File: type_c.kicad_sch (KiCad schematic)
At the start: 14 parts, among them U12 FUSB302B, U14 DPO2036

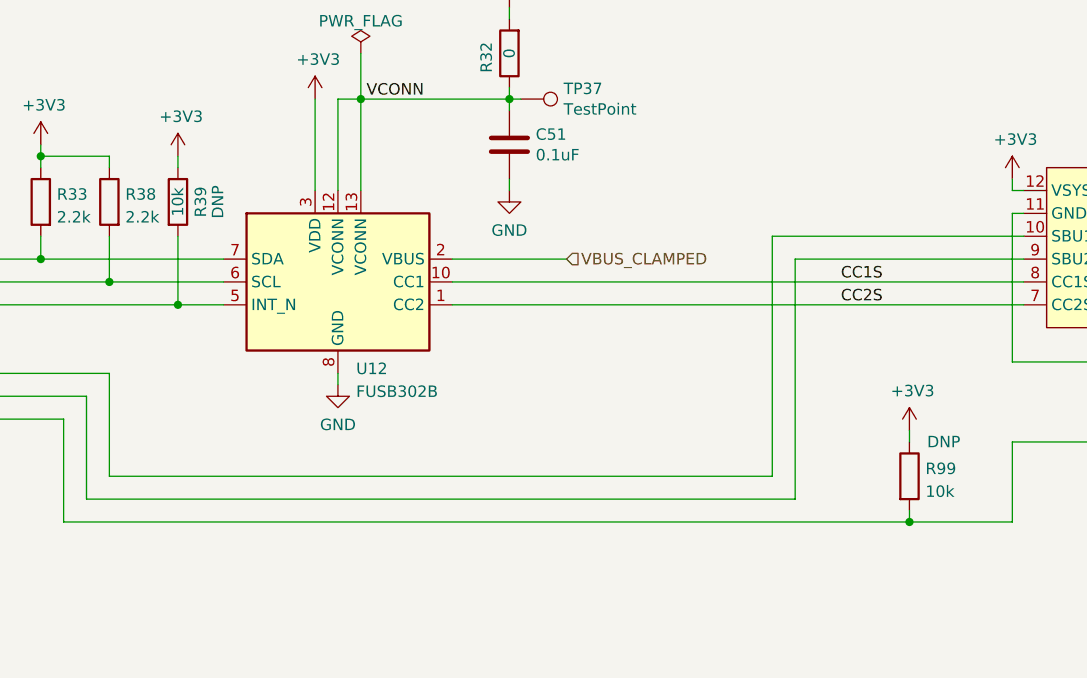
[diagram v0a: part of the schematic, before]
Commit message: add first round of hits on lcsc
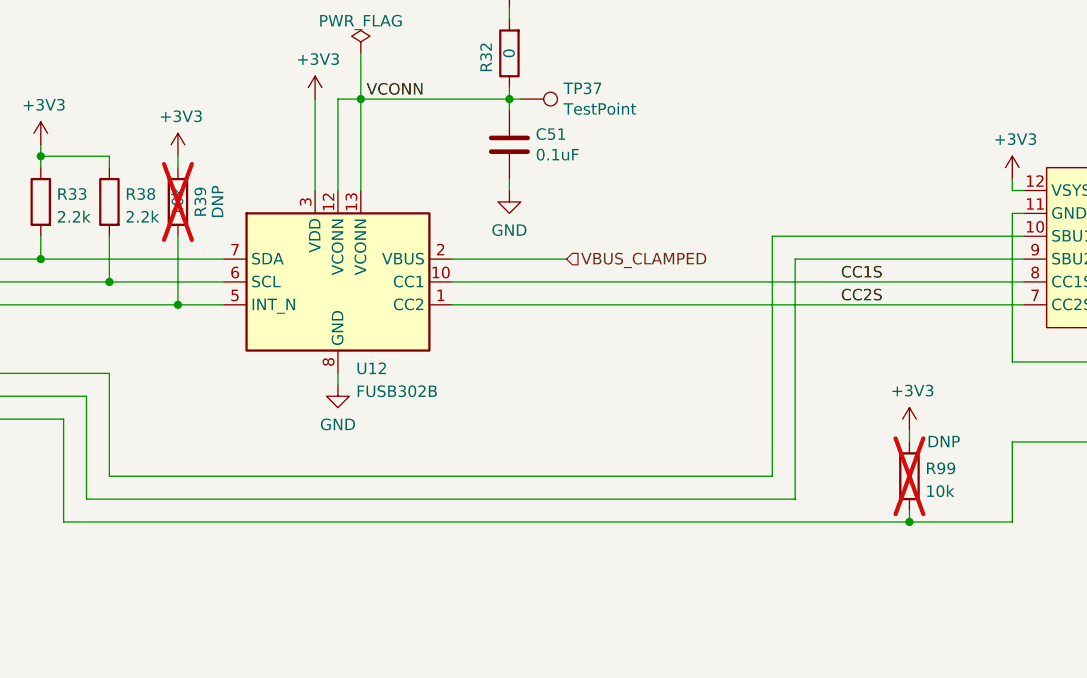
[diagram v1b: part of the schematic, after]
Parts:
- C49, C58: LCSC# (none) -> C318573
- C51, C63: LCSC# (none) -> C100072
- C52, C53: LCSC# (none) -> C13533
- R32: LCSC# (none) -> C106231
- R33, R38: LCSC# (none) -> C163447
- R39, R99: now not fitted
- U12: LCSC# (none) -> C132291
- U14: LCSC# (none) -> C3662892
